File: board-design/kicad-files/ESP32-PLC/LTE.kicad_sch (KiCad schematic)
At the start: 61 parts, among them J5 SF53S006VCBR2000, Q1 BC817, Q2 BC817, U3 EC21, U4 TXS0108EPW, U5 TXS0108EPW

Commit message: [UPDATE]
Work in progress.

Signed-off-by: Nicolae-Andrei Vasile <vasilenicolaeandrei@gmail.com>
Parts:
- gave numbers to parts that had none: 3
- renumbered C4 to C25, C4 to C26, C4 to C27, C4 to C28, C4 to C29, C5 to C30, C3 to C31, C3 to C32, C3 to C33, C3 to C34, C3 to C35, C3 to C36, C5 to C37, C4 to C38, C4 to C39, C4 to C40, C4 to C41, C4 to C42, C4 to C43, C4 to C44, C4 to C45, C4 to C46, C4 to C47, C4 to C48, D3 to D1, D4 to D2, J5 to J7, Q1 to Q3, Q2 to Q4, R5 to R39, R5 to R40, R5 to R41, R5 to R42, R9 to R44, R5 to R48, R5 to R49, R5 to R50, R5 to R51, R5 to R52, R5 to R53, R5 to R54, R5 to R55, R5 to R58, R5 to R59, RV3 to RV2, U3 to U4, U4 to U5, U5 to U6
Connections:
- net at C25.1, R39.1: now also D1.1 (IO1), J7.1 (VCC), U4.14 (USIM_VDD)
- net at R50.1: now also U5.17 (B3); no longer U5.15 (B5)
- net at R52.1: now also U5.15 (B5); no longer U5.17 (B3)
- net at R54.1: now also U5.13 (B7); no longer U5.20 (B1)
- net at R49.1: now also U5.18 (B2); no longer U5.14 (B6)
- net at R53.1: now also U5.14 (B6); no longer U5.18 (B2)
- net RI: now reaches U4.62 (RI)
- net RI: now also U5.8 (A7); no longer U5.1 (A1)
- net at R48.1: now also U5.20 (B1); no longer U5.13 (B7)
- net DCD: now reaches U4.63 (DCD)
- net DCD: now also U5.7 (A6); no longer U5.3 (A2)
- net CTS: now reaches U4.64 (CTS)
- net CTS: now also U5.6 (A5); no longer U5.4 (A3)
- net RTS: now reaches U4.65 (RTS), U5.5 (A4)
- net DTR: now reaches U4.66 (DTR)
- net DTR: now also U5.4 (A3); no longer U5.6 (A5)
- net TXD: now reaches U4.67 (TXD)
- net TXD: now also U5.3 (A2); no longer U5.7 (A6)
- net RXD: now reaches U4.68 (RXD)
- net RXD: now also U5.1 (A1); no longer U5.8 (A7)
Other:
- title: LTE -> ESP32
- moved on the sheet: R48, R49, R50, R52, R53, R54

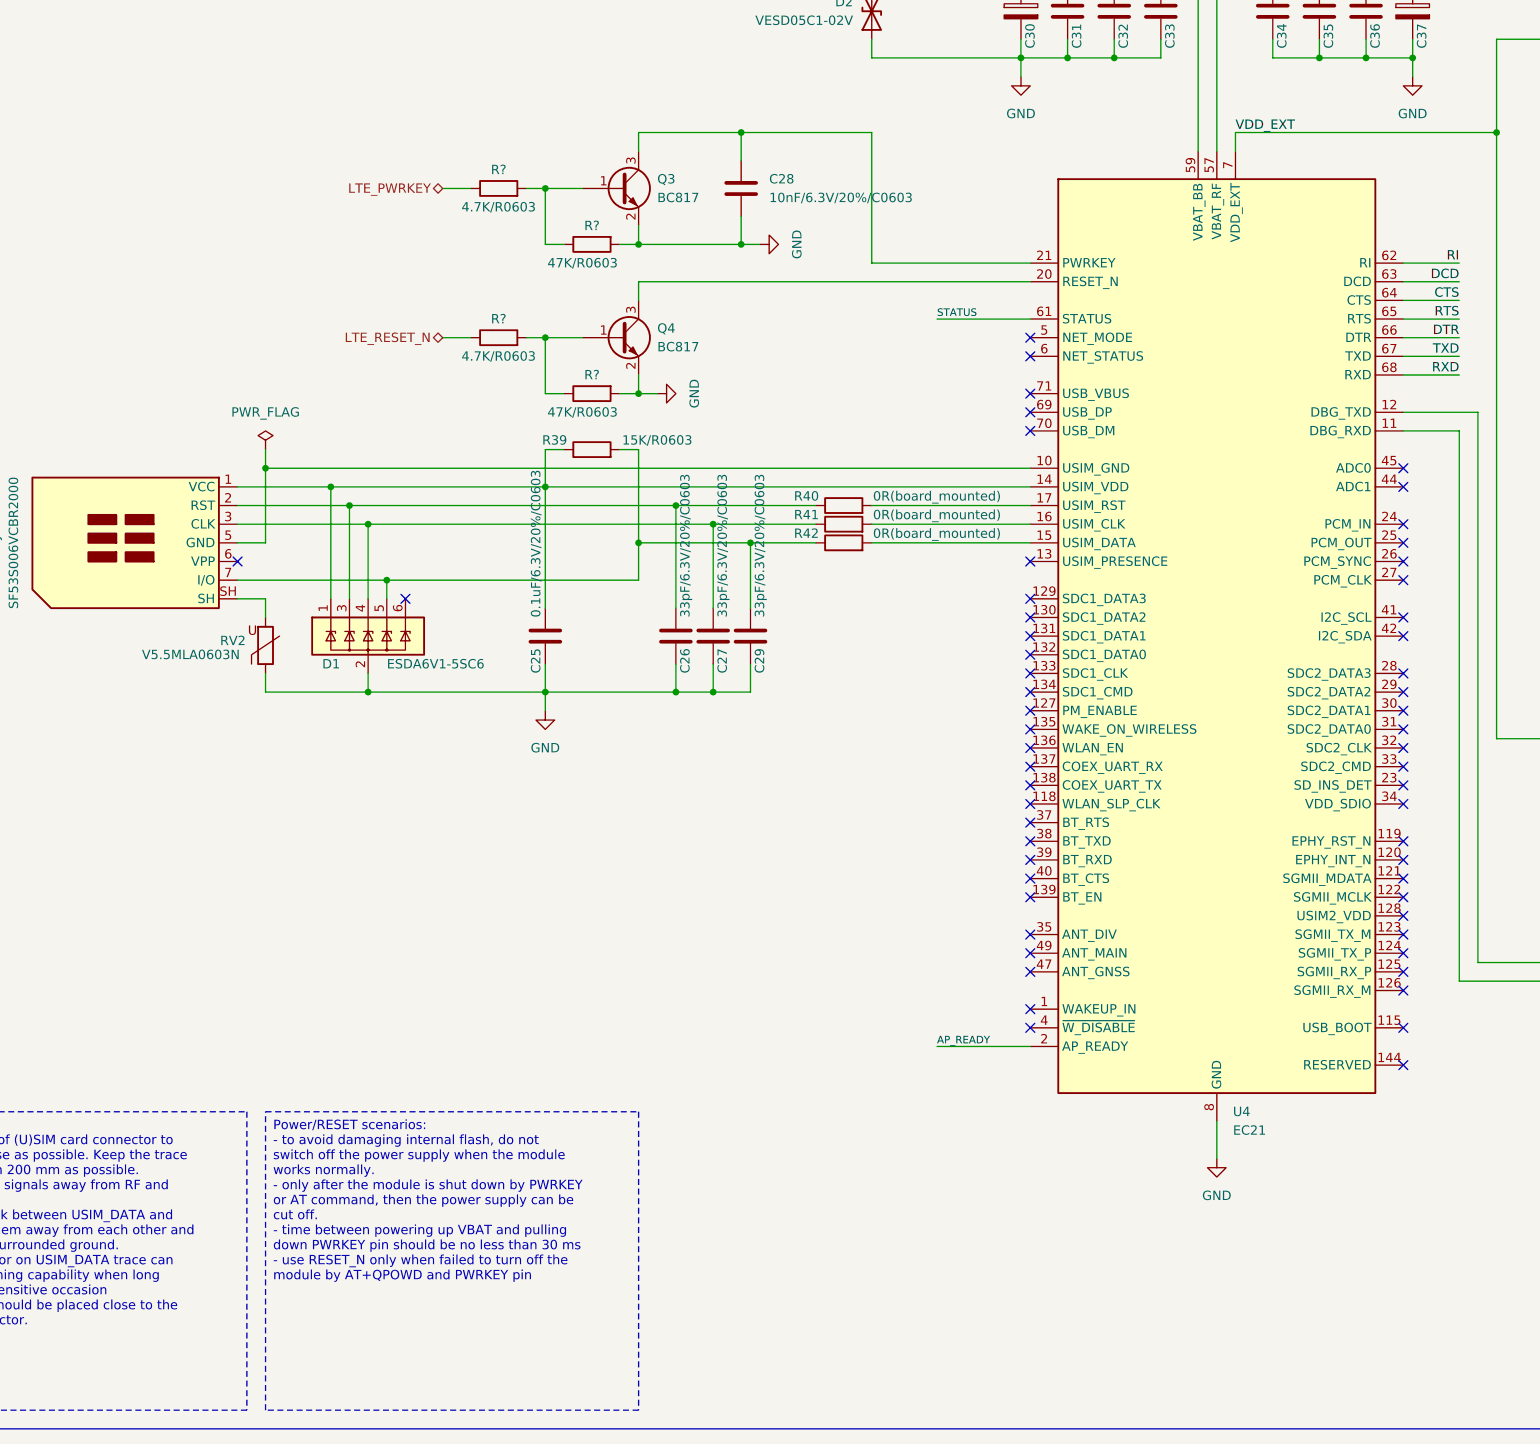
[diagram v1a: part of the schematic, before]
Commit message: [UPDATE]
Finished ESP32-PLC board design

Signed-off-by: Nicolae-Andrei Vasile <vasilenicolaeandrei@gmail.com>
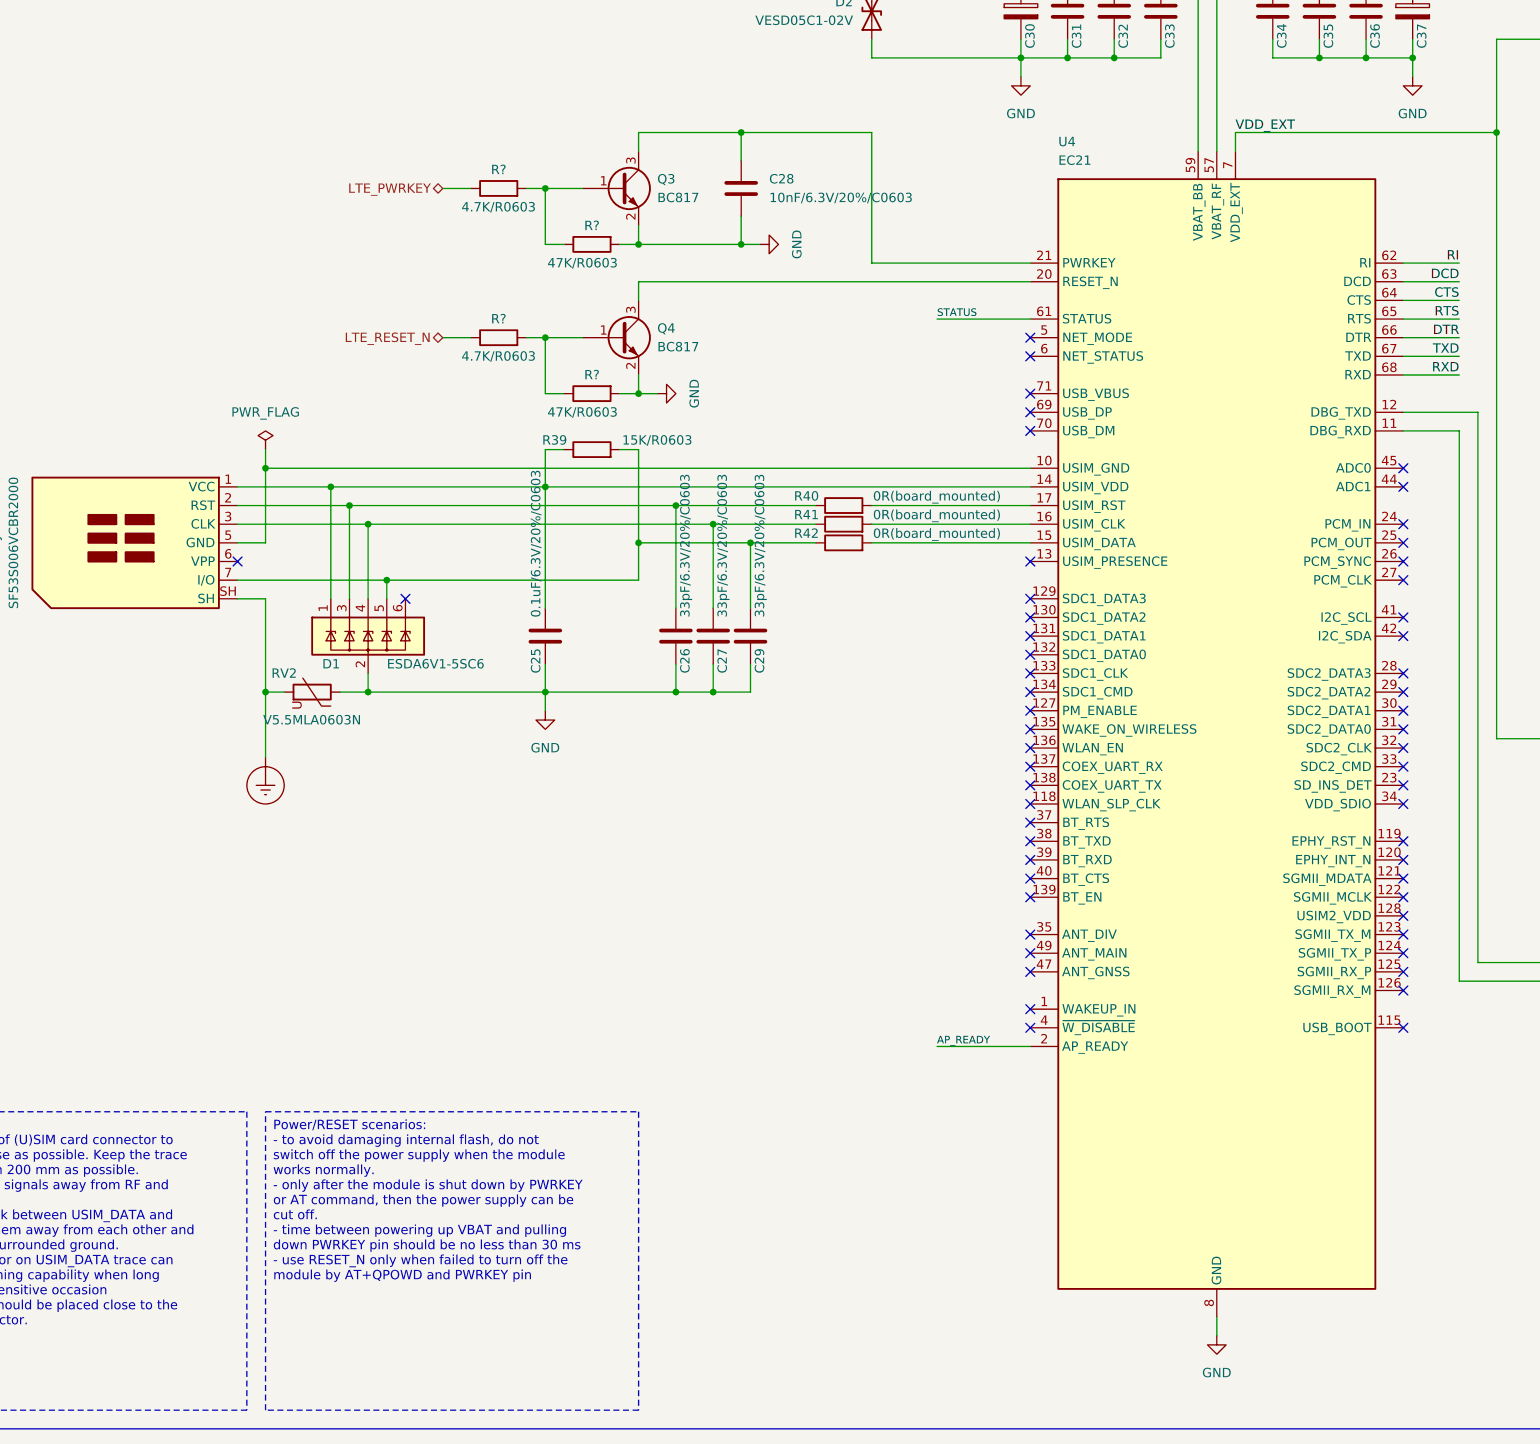
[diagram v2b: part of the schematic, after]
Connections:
- net Earth_Protective: now reaches J7.SH, RV2.2
- now unconnected: U4.113 (RESERVED), U4.114 (RESERVED), U4.116 (RESERVED), U4.117 (RESERVED), U4.140 (RESERVED), U4.141 (RESERVED), U4.142 (RESERVED), U4.143 (RESERVED), U4.144 (RESERVED), U4.18 (RESERVED), U4.3 (RESERVED), U4.43 (RESERVED), U4.55 (RESERVED)
- no-connect marks 57 -> 56
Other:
- moved on the sheet: RV2

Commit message: [Final report]
Added 3D models.

Signed-off-by: Nicolae-Andrei Vasile <vasilenicolaeandrei@gmail.com>
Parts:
- gave numbers to parts that had none: 10
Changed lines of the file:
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@@
   (symbol (lib_id "Device:R") (at 256.54 172.72 0) (mirror x) (unit 1)
     (in_bom yes) (on_board yes) (dnp no)
-    (property "Reference" "R?" (at 257.81 177.8 90)
+    (property "Reference" "R45" (at 257.81 177.8 90)
       (effects (font (size 1.27 1.27)))
     )
@@
     (instances
       (project "ESP32-PLC"
-        (path "/73e71d8b-00c7-414e-8d46-984de36f83d3"
-          (reference "R?") (unit 1)
-        )
-        (path "/73e71d8b-00c7-414e-8d46-984de36f83d3/153766c4-5539-4687-8dd8-c000826b4aca"
-          (reference "R23") (unit 1)
-        )
         (path "/73e71d8b-00c7-414e-8d46-984de36f83d3/c9284e56-31b2-4e73-96db-1ba1bc1f0222"
           (reference "R45") (unit 1)
@@
   (symbol (lib_id "Device:R") (at 299.72 208.28 0) (mirror x) (unit 1)
     (in_bom yes) (on_board yes) (dnp no)
-    (property "Reference" "R?" (at 300.99 213.36 90)
+    (property "Reference" "R56" (at 300.99 213.36 90)
       (effects (font (size 1.27 1.27)))
     )
@@
     (instances
       (project "ESP32-PLC"
-        (path "/73e71d8b-00c7-414e-8d46-984de36f83d3"
-          (reference "R?") (unit 1)
-        )
-        (path "/73e71d8b-00c7-414e-8d46-984de36f83d3/153766c4-5539-4687-8dd8-c000826b4aca"
-          (reference "R23") (unit 1)
-        )
         (path "/73e71d8b-00c7-414e-8d46-984de36f83d3/c9284e56-31b2-4e73-96db-1ba1bc1f0222"
           (reference "R56") (unit 1)
@@
   (symbol (lib_id "Device:R") (at 256.54 77.47 0) (mirror x) (unit 1)
     (in_bom yes) (on_board yes) (dnp no)
-    (property "Reference" "R?" (at 257.81 82.55 90)
+    (property "Reference" "R43" (at 257.81 82.55 90)
       (effects (font (size 1.27 1.27)))
     )
@@
     (instances
       (project "ESP32-PLC"
-        (path "/73e71d8b-00c7-414e-8d46-984de36f83d3"
-          (reference "R?") (unit 1)
-        )
-        (path "/73e71d8b-00c7-414e-8d46-984de36f83d3/153766c4-5539-4687-8dd8-c000826b4aca"
-          (reference "R23") (unit 1)
-        )
         (path "/73e71d8b-00c7-414e-8d46-984de36f83d3/c9284e56-31b2-4e73-96db-1ba1bc1f0222"
           (reference "R43") (unit 1)
@@
   (symbol (lib_id "Device:R") (at 256.54 208.28 180) (unit 1)
     (in_bom yes) (on_board yes) (dnp no)
-    (property "Reference" "R?" (at 255.27 213.36 90)
+    (property "Reference" "R46" (at 255.27 213.36 90)
       (effects (font (size 1.27 1.27)))
     )
@@
     (instances
       (project "ESP32-PLC"
-        (path "/73e71d8b-00c7-414e-8d46-984de36f83d3"
-          (reference "R?") (unit 1)
-        )
-        (path "/73e71d8b-00c7-414e-8d46-984de36f83d3/153766c4-5539-4687-8dd8-c000826b4aca"
-          (reference "R23") (unit 1)
-        )
         (path "/73e71d8b-00c7-414e-8d46-984de36f83d3/c9284e56-31b2-4e73-96db-1ba1bc1f0222"
           (reference "R46") (unit 1)
@@
   (symbol (lib_id "Device:R") (at 259.08 208.28 180) (unit 1)
     (in_bom yes) (on_board yes) (dnp no)
-    (property "Reference" "R?" (at 257.81 213.36 90)
+    (property "Reference" "R47" (at 257.81 213.36 90)
       (effects (font (size 1.27 1.27)))
     )
@@
     (instances
       (project "ESP32-PLC"
-        (path "/73e71d8b-00c7-414e-8d46-984de36f83d3"
-          (reference "R?") (unit 1)
-        )
-        (path "/73e71d8b-00c7-414e-8d46-984de36f83d3/153766c4-5539-4687-8dd8-c000826b4aca"
-          (reference "R23") (unit 1)
-        )
         (path "/73e71d8b-00c7-414e-8d46-984de36f83d3/c9284e56-31b2-4e73-96db-1ba1bc1f0222"
           (reference "R47") (unit 1)
@@
   (symbol (lib_id "Device:R") (at 118.11 86.36 90) (mirror x) (unit 1)
     (in_bom yes) (on_board yes) (dnp no)
-    (property "Reference" "R?" (at 118.11 83.82 90)
+    (property "Reference" "R37" (at 118.11 83.82 90)
       (effects (font (size 1.27 1.27)))
     )
@@
     (instances
       (project "ESP32-PLC"
-        (path "/73e71d8b-00c7-414e-8d46-984de36f83d3"
-          (reference "R?") (unit 1)
-        )
-        (path "/73e71d8b-00c7-414e-8d46-984de36f83d3/153766c4-5539-4687-8dd8-c000826b4aca"
-          (reference "R23") (unit 1)
-        )
         (path "/73e71d8b-00c7-414e-8d46-984de36f83d3/c9284e56-31b2-4e73-96db-1ba1bc1f0222"
           (reference "R37") (unit 1)
@@
   (symbol (lib_id "Device:R") (at 105.41 99.06 90) (unit 1)
     (in_bom yes) (on_board yes) (dnp no)
-    (property "Reference" "R?" (at 105.41 96.52 90)
+    (property "Reference" "R36" (at 105.41 96.52 90)
       (effects (font (size 1.27 1.27)))
     )
@@
     (instances
       (project "ESP32-PLC"
-        (path "/73e71d8b-00c7-414e-8d46-984de36f83d3"
-          (reference "R?") (unit 1)
-        )
-        (path "/73e71d8b-00c7-414e-8d46-984de36f83d3/153766c4-5539-4687-8dd8-c000826b4aca"
-          (reference "R23") (unit 1)
-        )
         (path "/73e71d8b-00c7-414e-8d46-984de36f83d3/c9284e56-31b2-4e73-96db-1ba1bc1f0222"
           (reference "R36") (unit 1)
@@
   (symbol (lib_id "Device:R") (at 321.31 172.72 180) (unit 1)
     (in_bom yes) (on_board yes) (dnp no)
-    (property "Reference" "R?" (at 320.04 177.8 90)
+    (property "Reference" "R57" (at 320.04 177.8 90)
       (effects (font (size 1.27 1.27)))
     )
@@
     (instances
       (project "ESP32-PLC"
-        (path "/73e71d8b-00c7-414e-8d46-984de36f83d3"
-          (reference "R?") (unit 1)
-        )
-        (path "/73e71d8b-00c7-414e-8d46-984de36f83d3/153766c4-5539-4687-8dd8-c000826b4aca"
-          (reference "R23") (unit 1)
-        )
         (path "/73e71d8b-00c7-414e-8d46-984de36f83d3/c9284e56-31b2-4e73-96db-1ba1bc1f0222"
           (reference "R57") (unit 1)
@@
   (symbol (lib_id "Device:R") (at 105.41 78.74 90) (unit 1)
     (in_bom yes) (on_board yes) (dnp no)
-    (property "Reference" "R?" (at 105.41 76.2 90)
+    (property "Reference" "R35" (at 105.41 76.2 90)
       (effects (font (size 1.27 1.27)))
     )
@@
     (instances
       (project "ESP32-PLC"
-        (path "/73e71d8b-00c7-414e-8d46-984de36f83d3"
-          (reference "R?") (unit 1)
-        )
-        (path "/73e71d8b-00c7-414e-8d46-984de36f83d3/153766c4-5539-4687-8dd8-c000826b4aca"
-          (reference "R23") (unit 1)
-        )
         (path "/73e71d8b-00c7-414e-8d46-984de36f83d3/c9284e56-31b2-4e73-96db-1ba1bc1f0222"
           (reference "R35") (unit 1)
@@
   (symbol (lib_id "power:Earth_Protective") (at 73.66 156.21 0) (unit 1)
     (in_bom yes) (on_board yes) (dnp no) (fields_autoplaced)
-    (property "Reference" "#PWR03" (at 80.01 162.56 0)
+    (property "Reference" "#PWR036" (at 80.01 162.56 0)
       (effects (font (size 1.27 1.27)) hide)
     )
@@
     (instances
       (project "ESP32-PLC"
-        (path "/73e71d8b-00c7-414e-8d46-984de36f83d3"
-          (reference "#PWR03") (unit 1)
-        )
         (path "/73e71d8b-00c7-414e-8d46-984de36f83d3/c9284e56-31b2-4e73-96db-1ba1bc1f0222"
           (reference "#PWR036") (unit 1)
@@
   (symbol (lib_id "Device:R") (at 118.11 106.68 90) (mirror x) (unit 1)
     (in_bom yes) (on_board yes) (dnp no)
-    (property "Reference" "R?" (at 118.11 104.14 90)
+    (property "Reference" "R38" (at 118.11 104.14 90)
       (effects (font (size 1.27 1.27)))
     )
@@
     (instances
       (project "ESP32-PLC"
-        (path "/73e71d8b-00c7-414e-8d46-984de36f83d3"
-          (reference "R?") (unit 1)
-        )
-        (path "/73e71d8b-00c7-414e-8d46-984de36f83d3/153766c4-5539-4687-8dd8-c000826b4aca"
-          (reference "R23") (unit 1)
-        )
         (path "/73e71d8b-00c7-414e-8d46-984de36f83d3/c9284e56-31b2-4e73-96db-1ba1bc1f0222"
           (reference "R38") (unit 1)
